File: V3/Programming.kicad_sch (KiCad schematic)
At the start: 12 parts

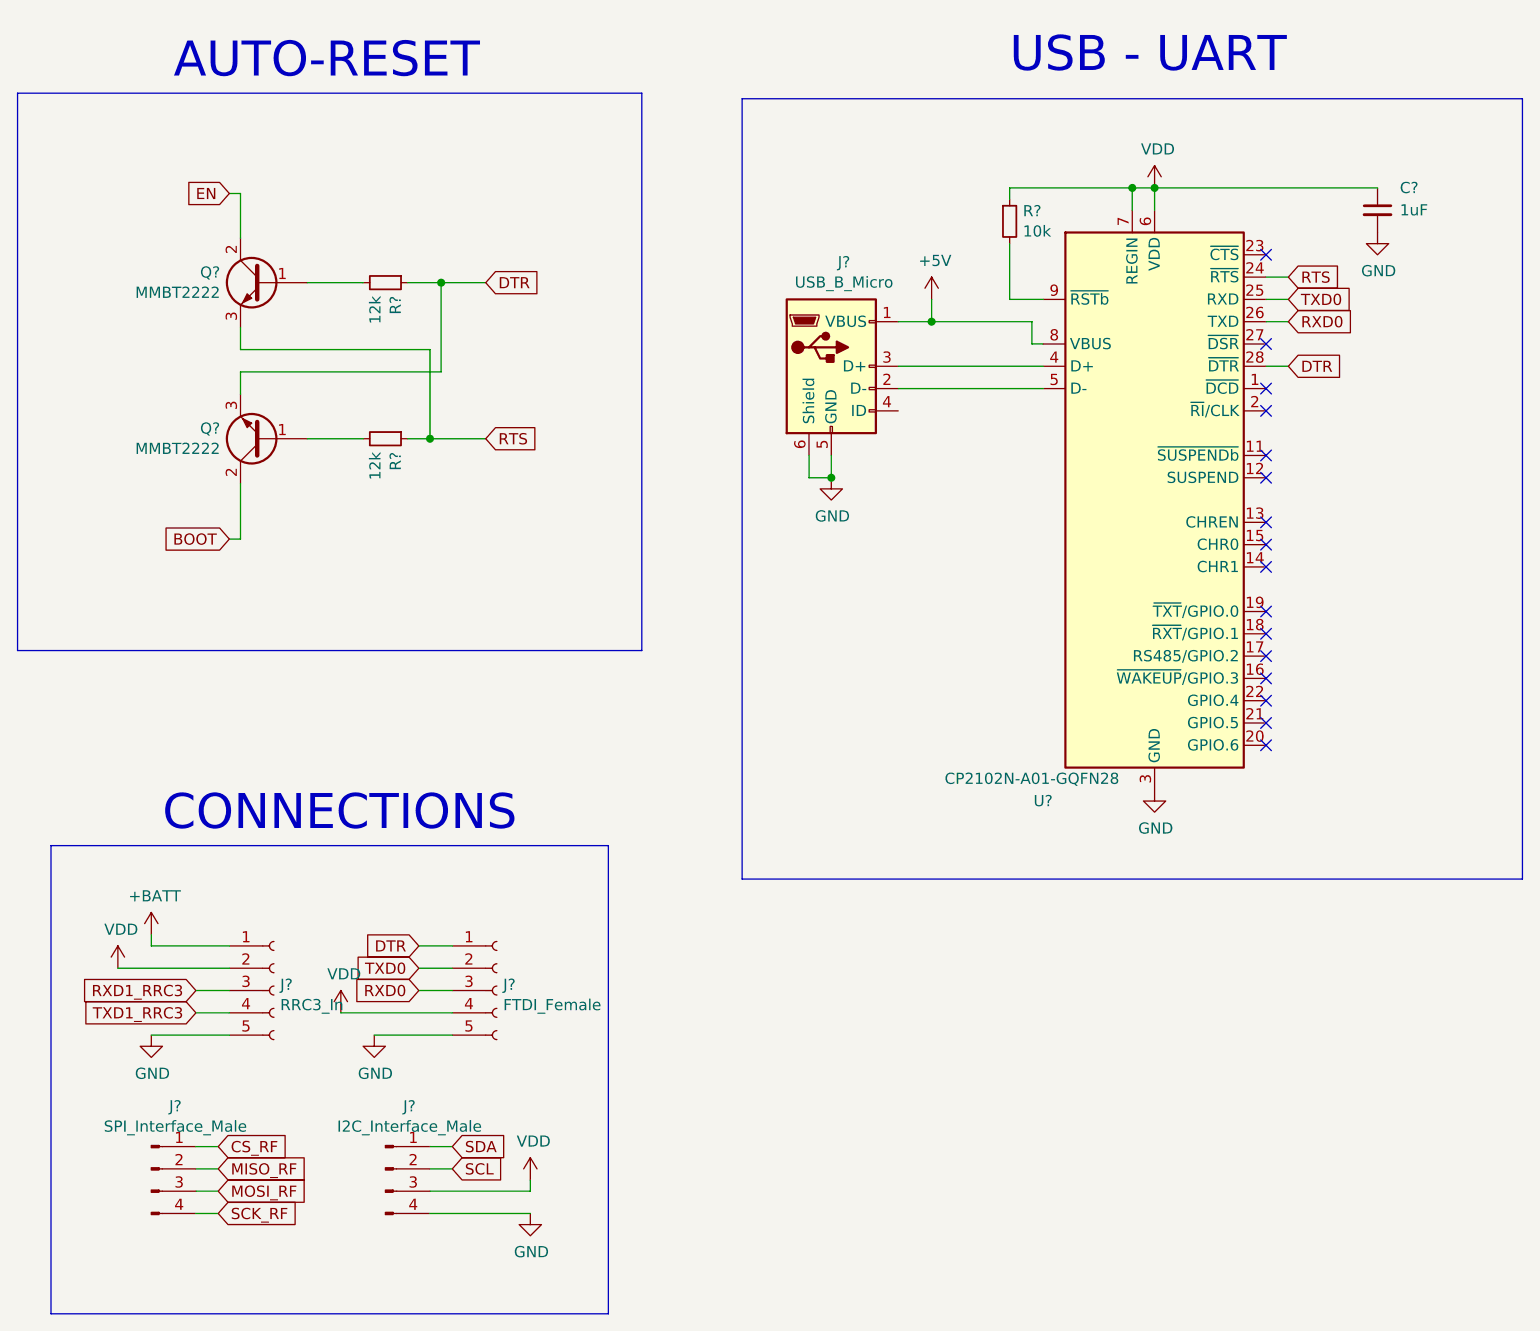
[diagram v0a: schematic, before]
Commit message: Added sims, updated V3 board
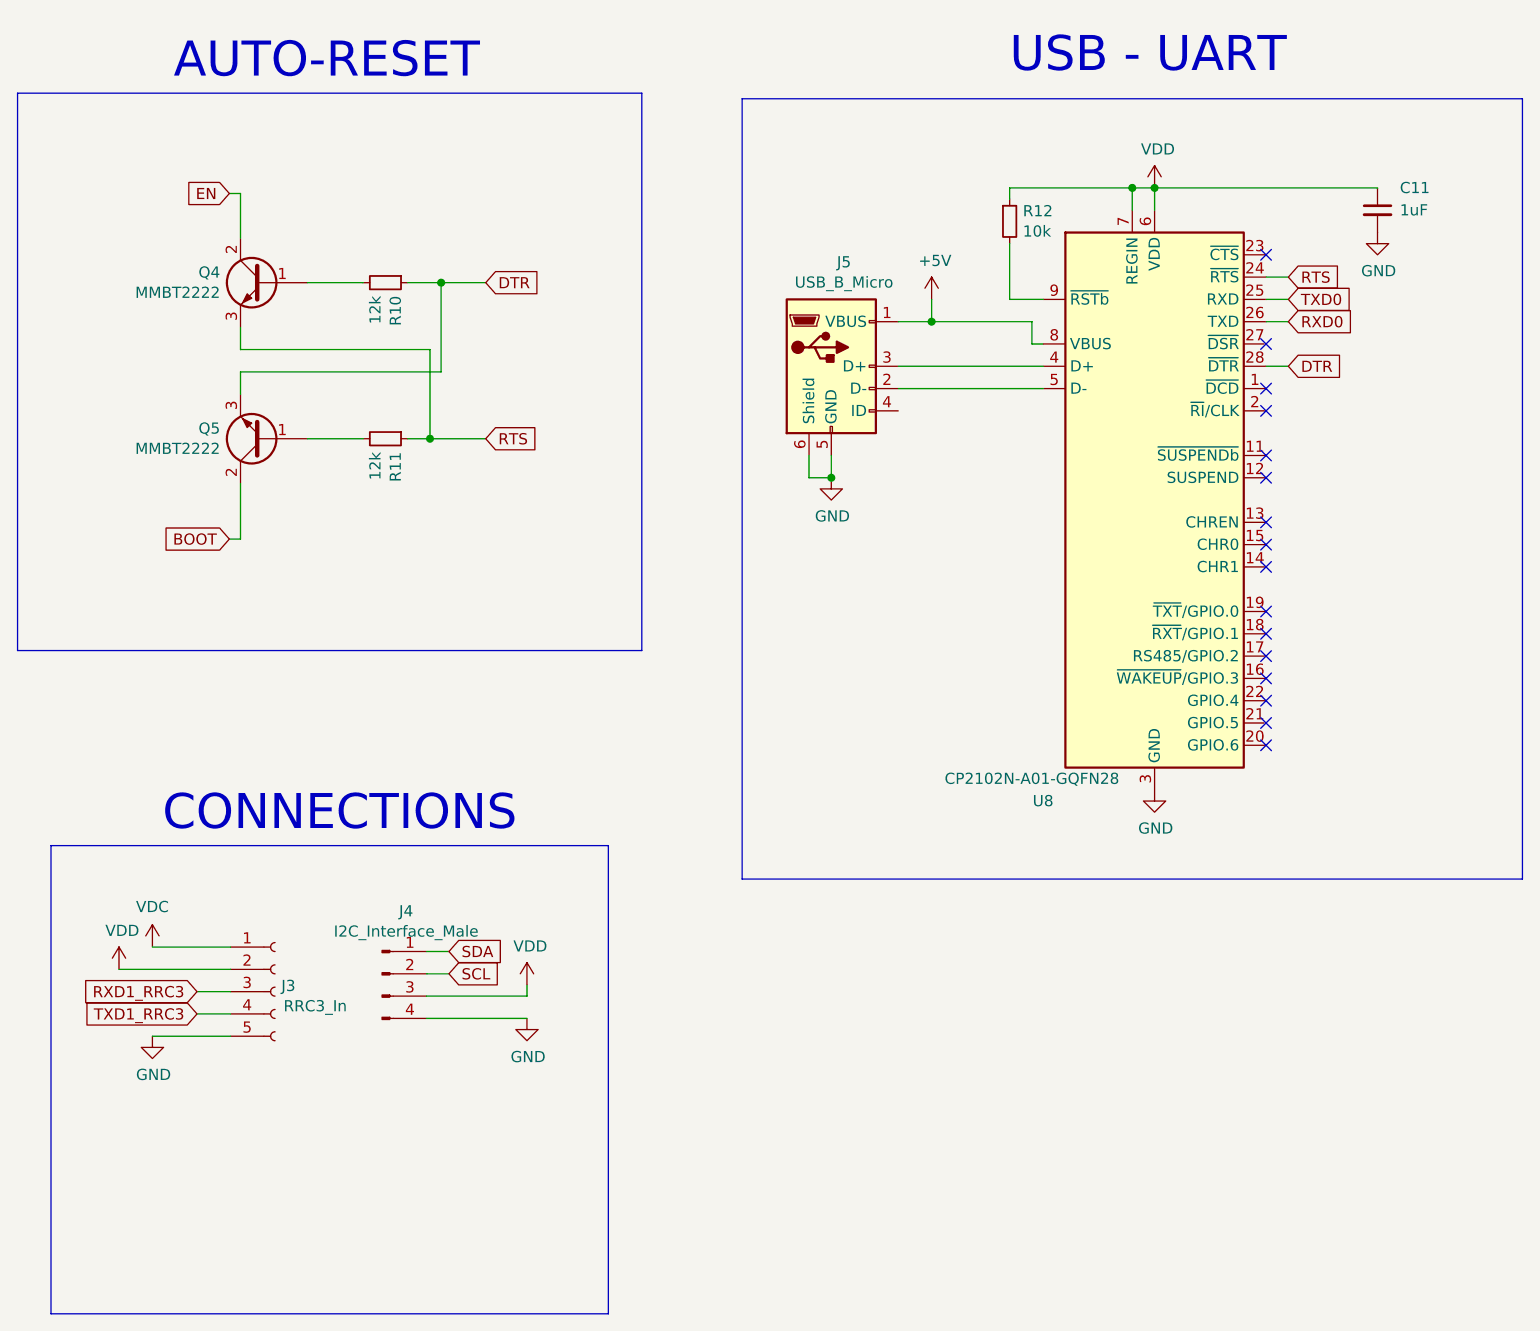
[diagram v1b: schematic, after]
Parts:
- removed J?: SPI_Interface_Male, Connector_PinHeader_2.54mm:PinHeader_1x04_P2.54mm_Vertical, symbol Connector:Conn_01x04_Male
- removed J?: FTDI_Female, Connector_PinHeader_2.54mm:PinHeader_1x05_P2.54mm_Vertical, symbol Connector:Conn_01x05_Female
- gave numbers to parts that had none: 10
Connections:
- net +BATT renamed VDC
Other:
- moved on the sheet: J4

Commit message: Updated costing sheet:
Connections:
- net VDC: no longer names the net of J3.1 (Pin_1)
- no-connect marks 16 -> 17
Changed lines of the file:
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@@
   (junction (at 160.655 38.735) (diameter 0) (color 0 0 0 0)
   )
+  (no_connect (at 46.482 125.222))
   (no_connect (at 173.355 102.235))
   (no_connect (at 173.355 99.695))
@@
       (effects (font (size 1.27 1.27)) hide)
     )
-    (pin "1")
-  )
-  (symbol (lib_id "power:VDC") (at 46.482 125.222 0) (unit 1)
-    (in_bom yes) (on_board yes) (fields_autoplaced)
-    (property "Reference" "#PWR0142" (id 0) (at 46.482 127.762 0)
-      (effects (font (size 1.27 1.27)) hide)
-    )
-    (property "Value" "VDC" (id 1) (at 46.482 120.65 0))
-    (property "Footprint" "" (id 2) (at 46.482 125.222 0)
-      (effects (font (size 1.27 1.27)) hide)
-    )
-    (property "Datasheet" "" (id 3) (at 46.482 125.222 0)
-      (effects (font (size 1.27 1.27)) hide)
-    )
